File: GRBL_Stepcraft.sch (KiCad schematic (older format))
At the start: 10 parts, among them J1 DB25_FEMALE, J2 CONN_01X02, P1 Power, P2 Analog, P3 Digital, P4 Digital, P5 CONN_01X01, P6 CONN_01X01, P7 CONN_01X01, P8 CONN_01X01

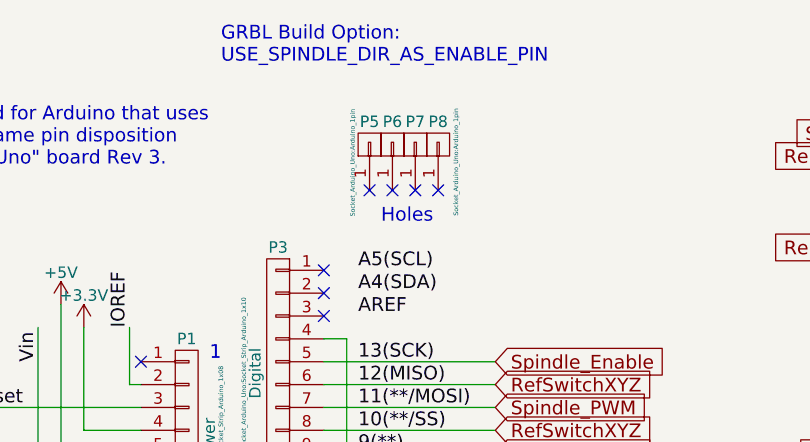
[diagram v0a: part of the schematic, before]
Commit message: grounded holes
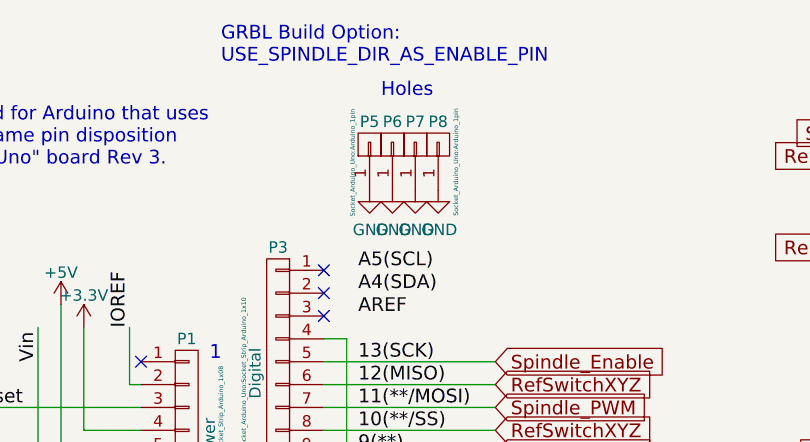
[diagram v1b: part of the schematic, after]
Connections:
- net GND: now also P5.1 (P1), P6.1 (P1), P7.1 (P1), P8.1 (P1)
- no-connect marks 11 -> 7
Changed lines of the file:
@@
 LIBS:contrib
 LIBS:valves
+LIBS:GRBL_Stepcraft-cache
 EELAYER 26 0
 EELAYER END
@@
 Text Label 4900 3400 0    60   ~ 0
 A5(SCL)
-Text Notes 5000 3200 0    60   ~ 0
+Text Notes 5000 2650 0    60   ~ 0
 Holes
 Text Notes 3100 2950 0    60   ~ 0
@@
 	0    -1   -1   0
 $EndComp
-NoConn ~ 4950 3050
-NoConn ~ 5050 3050
-NoConn ~ 5150 3050
-NoConn ~ 5250 3050
 $Comp
 L CONN_01X08 P4
@@
 	0    1    1    0
 $EndComp
+$Comp
+L GND #PWR?
+U 1 1 593DFBAD
+P 5250 3050
+F 0 "#PWR?" H 5250 2800 50  0001 C CNN
+F 1 "GND" H 5255 2877 50  0000 C CNN
+F 2 "" H 5250 3050 50  0001 C CNN
+F 3 "" H 5250 3050 50  0001 C CNN
+	1    5250 3050
+	1    0    0    -1
+$EndComp
+$Comp
+L GND #PWR?
+U 1 1 593DFBD3
+P 5150 3050
+F 0 "#PWR?" H 5150 2800 50  0001 C CNN
+F 1 "GND" H 5155 2877 50  0000 C CNN
+F 2 "" H 5150 3050 50  0001 C CNN
+F 3 "" H 5150 3050 50  0001 C CNN
+	1    5150 3050
+	1    0    0    -1
+$EndComp
+$Comp
+L GND #PWR?
+U 1 1 593DFBF2
+P 5050 3050
+F 0 "#PWR?" H 5050 2800 50  0001 C CNN
+F 1 "GND" H 5055 2877 50  0000 C CNN
+F 2 "" H 5050 3050 50  0001 C CNN
+F 3 "" H 5050 3050 50  0001 C CNN
+	1    5050 3050
+	1    0    0    -1
+$EndComp
+$Comp
+L GND #PWR?
+U 1 1 593DFC11
+P 4950 3050
+F 0 "#PWR?" H 4950 2800 50  0001 C CNN
+F 1 "GND" H 4955 2877 50  0000 C CNN
+F 2 "" H 4950 3050 50  0001 C CNN
+F 3 "" H 4950 3050 50  0001 C CNN
+	1    4950 3050
+	1    0    0    -1
+$EndComp
 $EndSCHEMATC
